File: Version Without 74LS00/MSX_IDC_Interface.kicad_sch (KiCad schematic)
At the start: 19 parts, among them J1 DE1 GPIO, U1 74LS00, U2 MSX_BUS, U3 74LVC245A, U4 74LVC245A, U5 74LVC245A, U6 74LVC245A, U7 74LVC245A

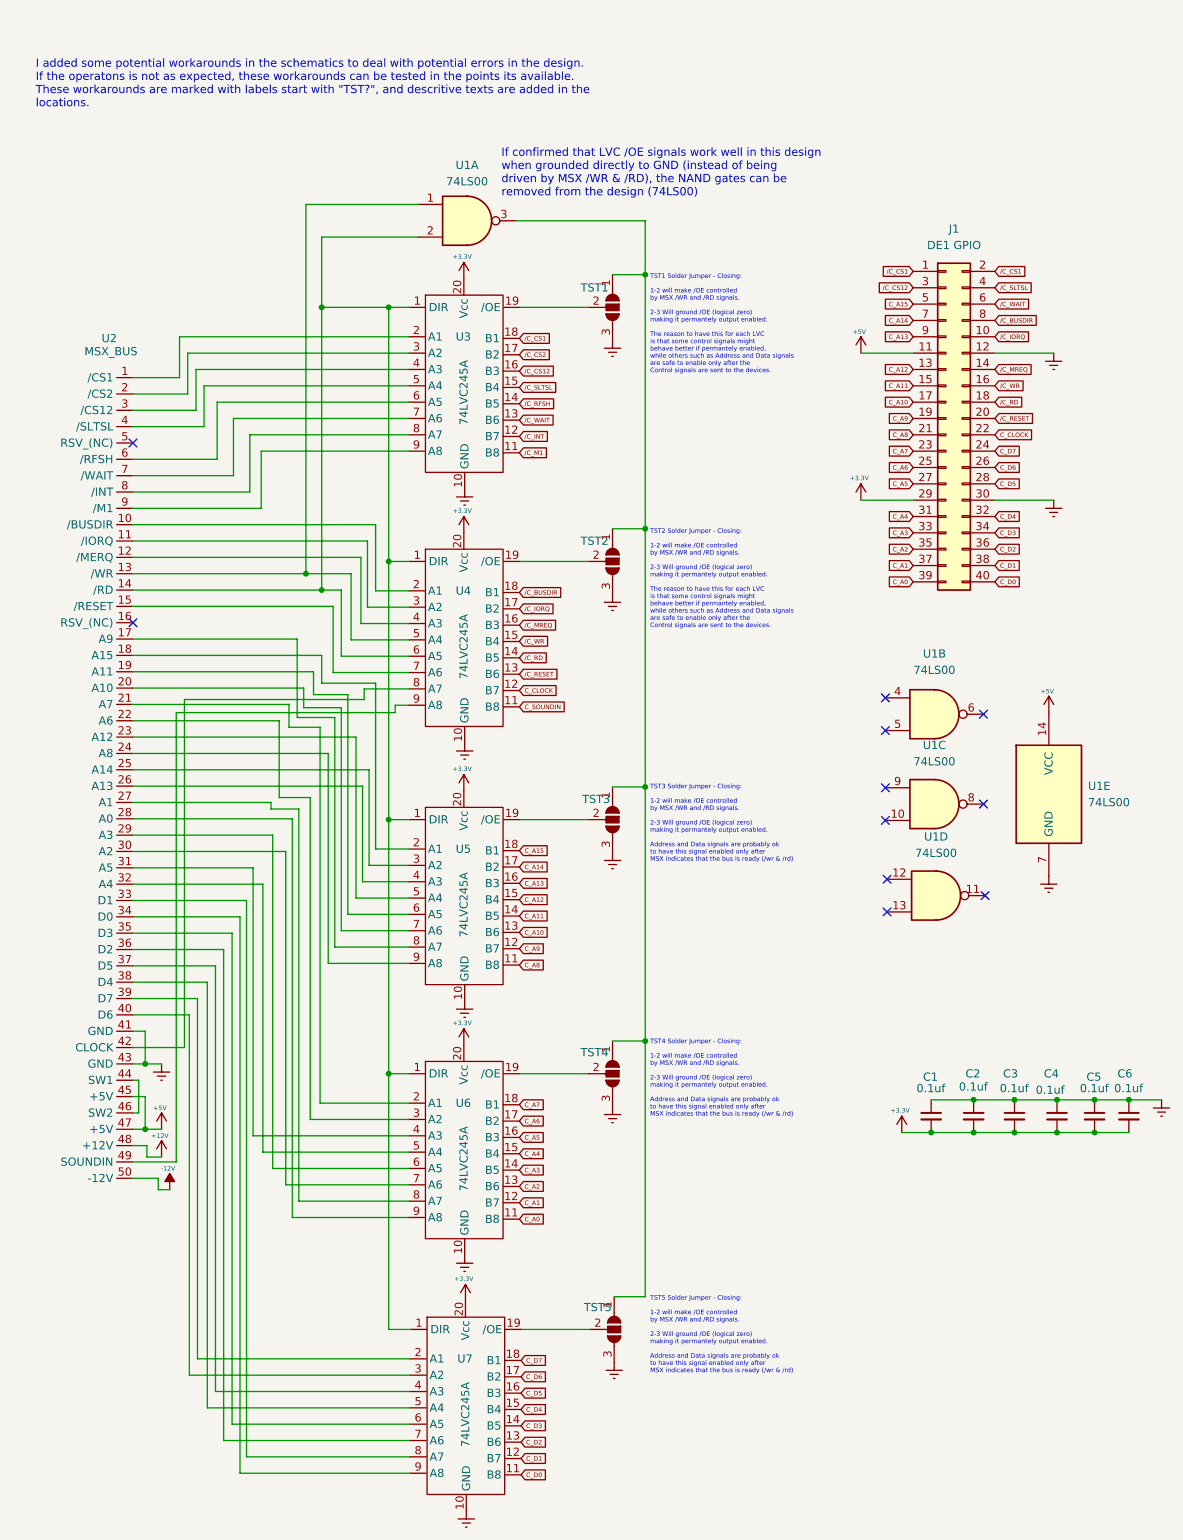
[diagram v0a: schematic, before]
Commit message: Changed the schematic to use a NAND port via transitors - to remove the 74LS00. Started routing the PCB
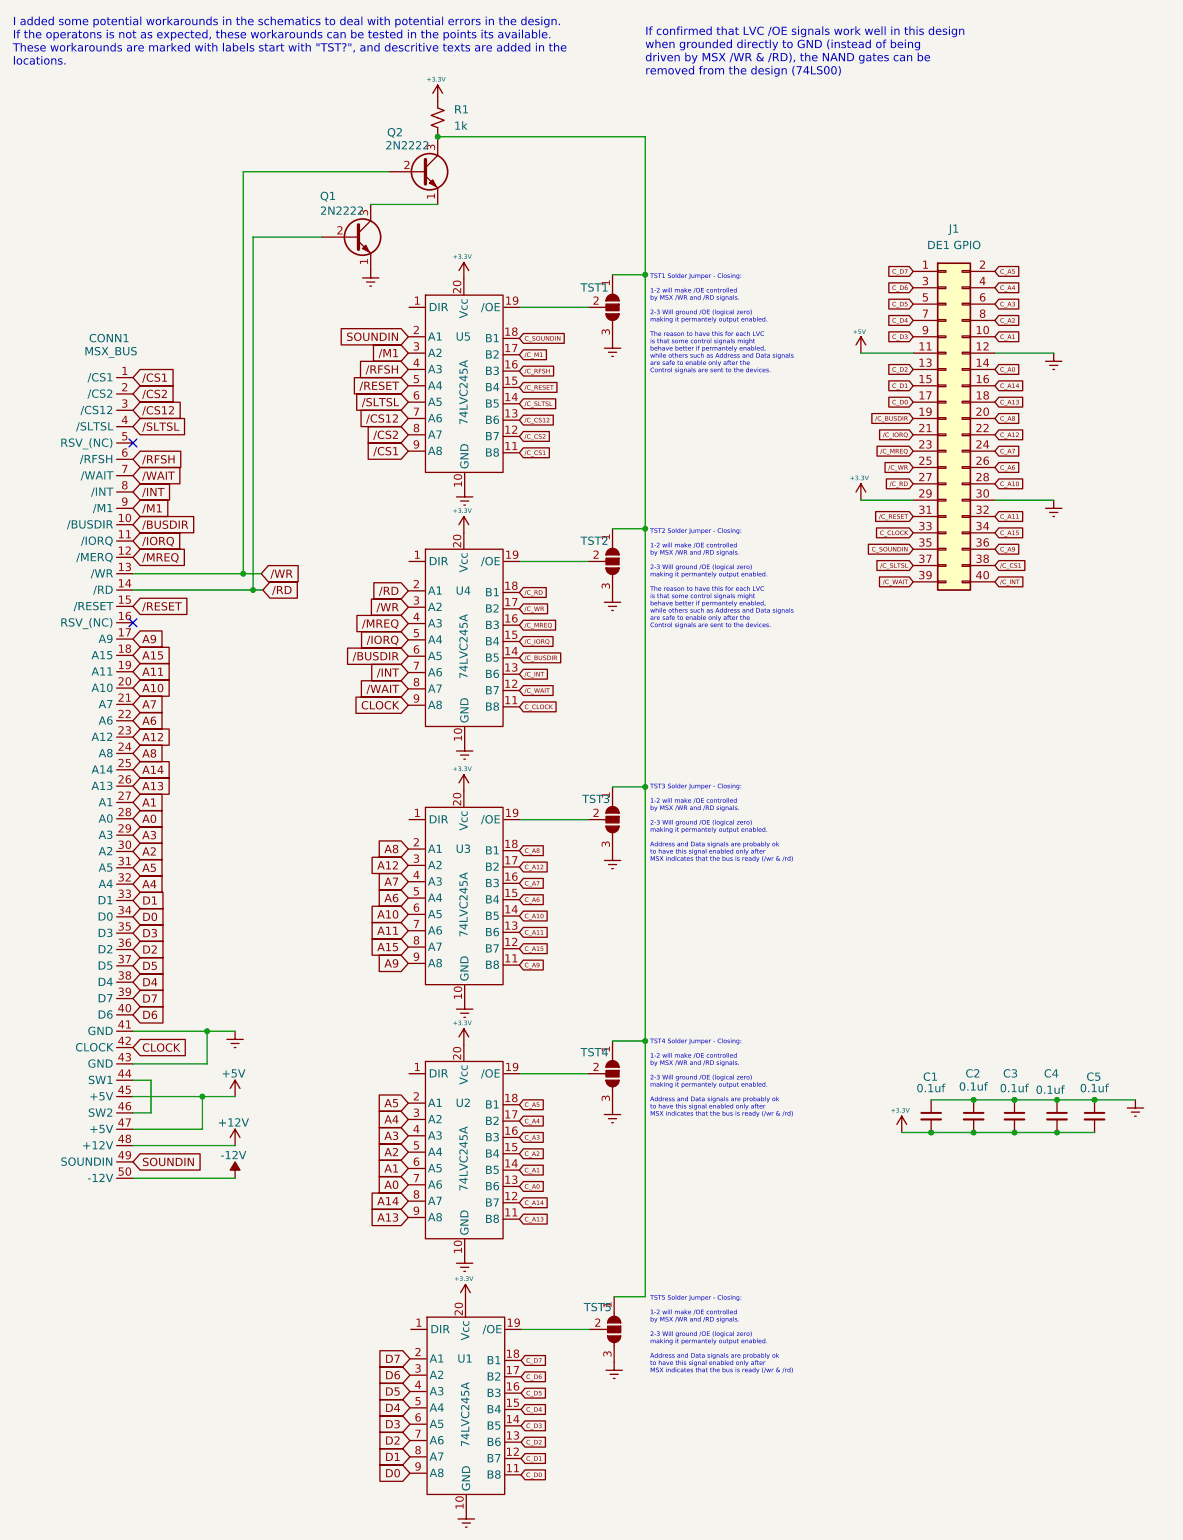
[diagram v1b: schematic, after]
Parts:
- removed C6: 0.1uf, Capacitor_THT:C_Disc_D3.0mm_W1.6mm_P2.50mm, symbol Device:C_Small
- removed U1: 74LS00, Package_DIP:DIP-14_W7.62mm, symbol 74xx:74LS00
- added Q1, Q2: 2N2222, Roni Footprints:TO127P584H533-3, symbol Transistor_BJT:2N2219
- added R1: 1k, Resistor_THT:R_Axial_DIN0207_L6.3mm_D2.5mm_P7.62mm_Horizontal, symbol Device:R_Small_US
- renumbered U2 to CONN1, U7 to U1, U6 to U2, U5 to U3, U3 to U5
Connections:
- net +3.3V: now also R1.1
- net C_A0: now also J1.14 (Pin_14), U2.13 (B6); no longer J1.39 (Pin_39), U2.11 (B8)
- net C_A1: now also J1.10 (Pin_10), U2.14 (B5); no longer J1.37 (Pin_37), U2.12 (B7)
- net C_A10: now also J1.28 (Pin_28), U3.14 (B5); no longer J1.17 (Pin_17), U3.13 (B6)
- net C_A11: now also J1.32 (Pin_32), U3.13 (B6); no longer J1.15 (Pin_15), U3.14 (B5)
- net C_A12: now also J1.22 (Pin_22), U3.17 (B2); no longer J1.13 (Pin_13), U3.15 (B4)
- net C_A13: now also J1.18 (Pin_18), U2.11 (B8); no longer J1.9 (Pin_9), U3.16 (B3)
- net C_A14: now also J1.16 (Pin_16), U2.12 (B7); no longer J1.7 (Pin_7), U3.17 (B2)
- net C_A15: now also J1.34 (Pin_34), U3.12 (B7); no longer J1.5 (Pin_5), U3.18 (B1)
- net C_A2: now also J1.8 (Pin_8), U2.15 (B4); no longer J1.35 (Pin_35), U2.13 (B6)
- net C_A3: now also J1.6 (Pin_6), U2.16 (B3); no longer J1.33 (Pin_33), U2.14 (B5)
- net C_A4: now also J1.4 (Pin_4), U2.17 (B2); no longer J1.31 (Pin_31), U2.15 (B4)
- net C_A5: now also J1.2 (Pin_2), U2.18 (B1); no longer J1.27 (Pin_27), U2.16 (B3)
- net C_A6: now also J1.26 (Pin_26), U3.15 (B4); no longer J1.25 (Pin_25), U2.17 (B2)
- net C_A7: now also J1.24 (Pin_24), U3.16 (B3); no longer J1.23 (Pin_23), U2.18 (B1)
- net C_A8: now also J1.20 (Pin_20), U3.18 (B1); no longer J1.21 (Pin_21), U3.11 (B8)
- net C_A9: now also J1.36 (Pin_36), U3.11 (B8); no longer J1.19 (Pin_19), U3.12 (B7)
- net C_CLOCK: now also J1.33 (Pin_33), U4.11 (B8); no longer J1.22 (Pin_22), U4.12 (B7)
- net C_D0: now also J1.17 (Pin_17); no longer J1.40 (Pin_40)
- net C_D1: now also J1.15 (Pin_15); no longer J1.38 (Pin_38)
- net C_D2: now also J1.13 (Pin_13); no longer J1.36 (Pin_36)
- net C_D3: now also J1.9 (Pin_9); no longer J1.34 (Pin_34)
- net C_D4: now also J1.7 (Pin_7); no longer J1.32 (Pin_32)
- net C_D5: now also J1.5 (Pin_5); no longer J1.28 (Pin_28)
- net C_D6: now also J1.3 (Pin_3); no longer J1.26 (Pin_26)
- net C_D7: now also J1.1 (Pin_1); no longer J1.24 (Pin_24)
- net C_SOUNDIN: now also J1.35 (Pin_35), U5.18 (B1); no longer U4.11 (B8)
- net GNDREF: now also Q1.1 (E)
- net /C_BUSDIR: now also J1.19 (Pin_19), U4.14 (B5); no longer J1.8 (Pin_8), U4.18 (B1)
- net /C_CS1: now also J1.38 (Pin_38), U5.11 (B8); no longer J1.1 (Pin_1), J1.2 (Pin_2), U5.18 (B1)
- net /C_CS12: now also U5.13 (B6); no longer J1.3 (Pin_3), U5.16 (B3)
- net /C_CS2: now also U5.12 (B7); no longer U5.17 (B2)
- net /C_INT: now also J1.40 (Pin_40), U4.13 (B6); no longer U5.12 (B7)
- net /C_IORQ: now also J1.21 (Pin_21), U4.15 (B4); no longer J1.10 (Pin_10), U4.17 (B2)
- net /C_M1: now also U5.17 (B2); no longer U5.11 (B8)
- net /C_MREQ: now also J1.23 (Pin_23); no longer J1.14 (Pin_14)
- net /C_RD: now also J1.27 (Pin_27), U4.18 (B1); no longer J1.18 (Pin_18), U4.14 (B5)
- net /C_RESET: now also J1.31 (Pin_31), U5.15 (B4); no longer J1.20 (Pin_20), U4.13 (B6)
- net /C_RFSH: now also U5.16 (B3); no longer U5.14 (B5)
- net /C_SLTSL: now also J1.37 (Pin_37), U5.14 (B5); no longer J1.4 (Pin_4), U5.15 (B4)
- net /C_WAIT: now also J1.39 (Pin_39), U4.12 (B7); no longer J1.6 (Pin_6), U5.13 (B6)
- net /C_WR: now also J1.25 (Pin_25), U4.17 (B2); no longer J1.16 (Pin_16)
- net at TST1.1 (A), TST2.1 (A), TST3.1 (A)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: now also Q2.3 (C), R1.2
- net SOUNDIN: now reaches U5.2 (A1)
- net SOUNDIN: now also CONN1.49 (SOUNDIN); no longer CONN1.1 (/CS1)
- net /CS2: now reaches CONN1.2 (/CS2)
- net /CS2: now also U5.8 (A7); no longer U5.3 (A2)
- net /CS12: now reaches CONN1.3 (/CS12)
- net /CS12: now also U5.7 (A6); no longer U5.4 (A3)
- net /RESET: now reaches U5.5 (A4)
- net /RESET: now also CONN1.15 (/RESET); no longer CONN1.4 (/SLTSL)
- net /RFSH: now reaches CONN1.6 (/RFSH)
- net /RFSH: now also U5.4 (A3); no longer U5.6 (A5)
- net /WAIT: now reaches CONN1.7 (/WAIT)
- net /WAIT: now also U4.8 (A7); no longer U5.7 (A6)
- net /INT: now reaches CONN1.8 (/INT)
- net /INT: now also U4.7 (A6); no longer U5.8 (A7)
- net /CS1: now reaches U5.9 (A8)
- net /CS1: now also CONN1.1 (/CS1); no longer CONN1.9 (/M1)
- net /BUSDIR: now reaches CONN1.10 (/BUSDIR)
- net /BUSDIR: now also U4.6 (A5); no longer U4.2 (A1)
- net /IORQ: now reaches CONN1.11 (/IORQ)
- net /IORQ: now also U4.5 (A4); no longer U4.3 (A2)
- net /MREQ: now reaches CONN1.12 (/MERQ), U4.4 (A3)
- net /WR: now reaches CONN1.13 (/WR)
- net /WR: now also U4.3 (A2), Q2.2 (B); no longer U4.5 (A4)
- net A15: now reaches U3.8 (A7)
- net A15: now also CONN1.18 (A15); no longer CONN1.17 (A9)
- net A8: now reaches U3.2 (A1)
- net A8: now also CONN1.24 (A8); no longer CONN1.18 (A15)
- net A10: now reaches U3.6 (A5)
- net A10: now also CONN1.20 (A10); no longer CONN1.19 (A11)
- net A11: now reaches U3.7 (A6)
- net A11: now also CONN1.19 (A11); no longer CONN1.20 (A10)
- net A5: now reaches U2.2 (A1)
- net A5: now also CONN1.31 (A5); no longer CONN1.21 (A7)
- net A4: now reaches U2.3 (A2)
- net A4: now also CONN1.32 (A4); no longer CONN1.22 (A6)
- net A12: now reaches CONN1.23 (A12)
- net A12: now also U3.3 (A2); no longer U3.5 (A4)
- net A9: now reaches U3.9 (A8)
- net A9: now also CONN1.17 (A9); no longer CONN1.24 (A8)
- net A14: now reaches CONN1.25 (A14)
- net A14: now also U2.8 (A7); no longer U3.3 (A2)
- net A13: now reaches CONN1.26 (A13)
- net A13: now also U2.9 (A8); no longer U3.4 (A3)
- net A1: now reaches CONN1.27 (A1)
- net A1: now also U2.6 (A5); no longer U2.8 (A7)
- net A0: now reaches CONN1.28 (A0)
- net A0: now also U2.7 (A6); no longer U2.9 (A8)
- net A3: now reaches CONN1.29 (A3)
- net A3: now also U2.4 (A3); no longer U2.6 (A5)
- net A2: now reaches CONN1.30 (A2)
- net A2: now also U2.5 (A4); no longer U2.7 (A6)
- net D1: now reaches CONN1.33 (D1), U1.8 (A7)
- net D0: now reaches CONN1.34 (D0), U1.9 (A8)
- net D3: now reaches CONN1.35 (D3), U1.6 (A5)
- net D2: now reaches CONN1.36 (D2), U1.7 (A6)
- net D5: now reaches CONN1.37 (D5), U1.4 (A3)
- net D4: now reaches CONN1.38 (D4), U1.5 (A4)
- net D7: now reaches CONN1.39 (D7), U1.2 (A1)
- net D6: now reaches CONN1.40 (D6), U1.3 (A2)
- net CLOCK: now reaches CONN1.42 (CLOCK)
- net CLOCK: now also U4.9 (A8); no longer U4.8 (A7)
- new net: Q1.3 (C), Q2.1 (E)
- new net A6: CONN1.22 (A6), U3.5 (A4)
- new net A7: CONN1.21 (A7), U3.4 (A3)
- new net /M1: CONN1.9 (/M1), U5.3 (A2)
- new net /RD: CONN1.14 (/RD), Q1.2 (B), U4.2 (A1)
- new net /SLTSL: CONN1.4 (/SLTSL), U5.6 (A5)
- now unconnected: U1.1 (DIR), U2.1 (DIR), U3.1 (DIR), U4.1 (DIR), U5.1 (DIR)
- no-connect marks 11 -> 2
